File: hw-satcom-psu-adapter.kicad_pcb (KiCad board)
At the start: 2 copper layers, 148.9 x 85.2 mm, 87 parts, among them J1 XT60, J2 ATX-24, J3 Conn_02x02_Top_Bottom, J4 Conn_02x02_Top_Bottom, Q2 KIA3510AD, Q5 2N7002, Q6 2N7002, U1 Brick-DCDC, U10 ZXDN10, U2 LM5067, U3 EL3H7(B)(TA)-G, U4 EL3H7(B)(TA)-G, U5 AV10-48S05, U6 EL3H7(B)(TA)-G, U7 TPS3510, U8 ZXDN10, U9 ZXDN10

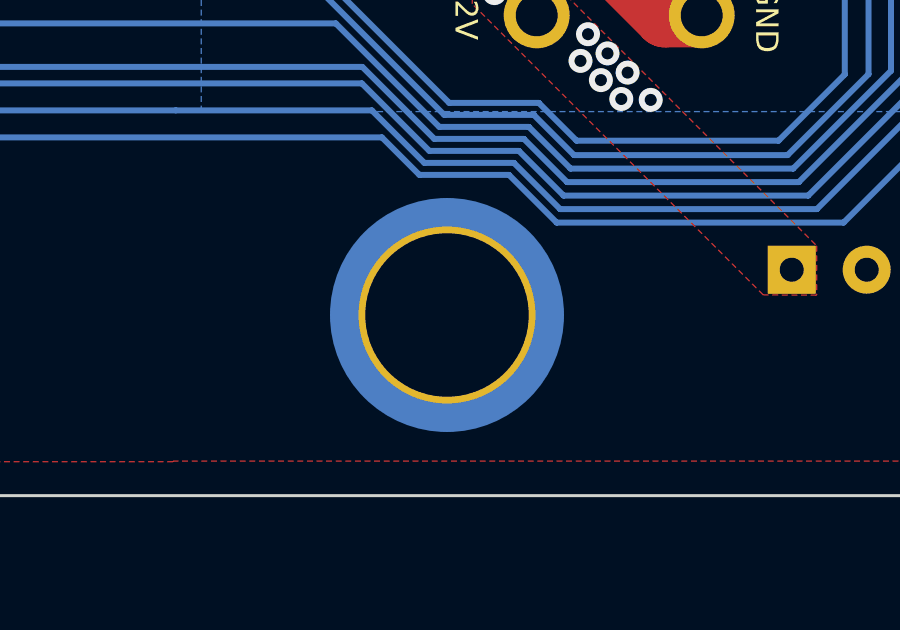
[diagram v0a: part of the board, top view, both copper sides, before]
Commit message: Adjust screw hole position
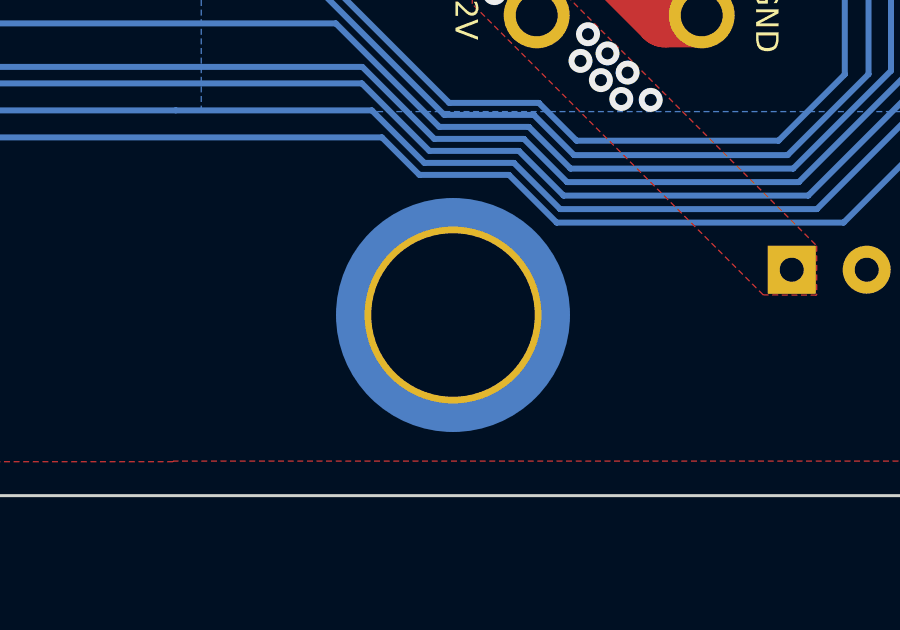
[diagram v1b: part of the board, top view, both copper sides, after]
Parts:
- moved H7 0.20 mm to (205.6, 129.7)
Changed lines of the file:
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@@
   )
   (footprint "t123yh:MountingHole_SMTSO-632" locked (layer "B.Cu")
-    (at 205.39 129.72 180)
+    (at 205.59 129.72 180)
     (descr "Screw Hole 6#32")
     (property "Sheetfile" "文件： hw-satcom-psu-adapter.kicad_sch")

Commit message: Reduce LED brightness
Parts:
- R14, R9: value 56k -> 68k
- R22: value 8.2k -> 10k
- R7, R8: value 5.1k -> 6.8k
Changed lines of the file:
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@@
       (effects (font (size 1 1) (thickness 0.15)))
     )
-    (fp_text value "56k" (at 0.136657 3.388724) (layer "F.Fab")
+    (fp_text value "68k" (at 0.136657 3.388724) (layer "F.Fab")
       (effects (font (size 1 1) (thickness 0.15)))
     )
@@
       (effects (font (size 1 1) (thickness 0.15)))
     )
-    (fp_text value "8.2k" (at 0.696657 3.173724 90) (layer "F.Fab")
+    (fp_text value "10k" (at 0.696657 3.173724 90) (layer "F.Fab")
       (effects (font (size 1 1) (thickness 0.15)))
     )
@@
       (effects (font (size 1 1) (thickness 0.15)))
     )
-    (fp_text value "5.1k" (at 0.696657 3.173724) (layer "F.Fab")
+    (fp_text value "6.8k" (at 0.696657 3.173724) (layer "F.Fab")
       (effects (font (size 1 1) (thickness 0.15)))
     )
@@
       (effects (font (size 1 1) (thickness 0.15)))
     )
-    (fp_text value "56k" (at 0.136657 3.388724 -270) (layer "F.Fab")
+    (fp_text value "68k" (at 0.136657 3.388724 -270) (layer "F.Fab")
       (effects (font (size 1 1) (thickness 0.15)))
     )
@@
       (effects (font (size 1 1) (thickness 0.15)))
     )
-    (fp_text value "5.1k" (at 0.696657 3.173724) (layer "F.Fab")
-      (effects (font (size 1 1) (thickness 0.15)))
-    )
+    (fp_text value "6.8k" (at 0.696657 3.173724) (layer "F.Fab")
+      (effects (font (size 1 1) (thickness 0.15)))
+    )

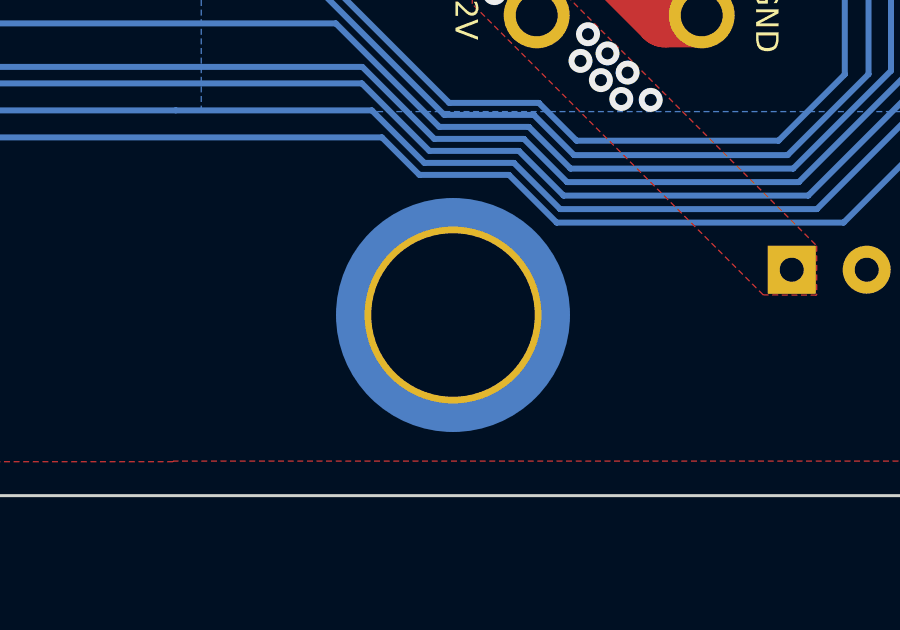
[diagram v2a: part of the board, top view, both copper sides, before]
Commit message: Revert "Adjust screw hole position"
This reverts commit 63cac71901258e286d442f6c161a0cf4eb18ce6f.
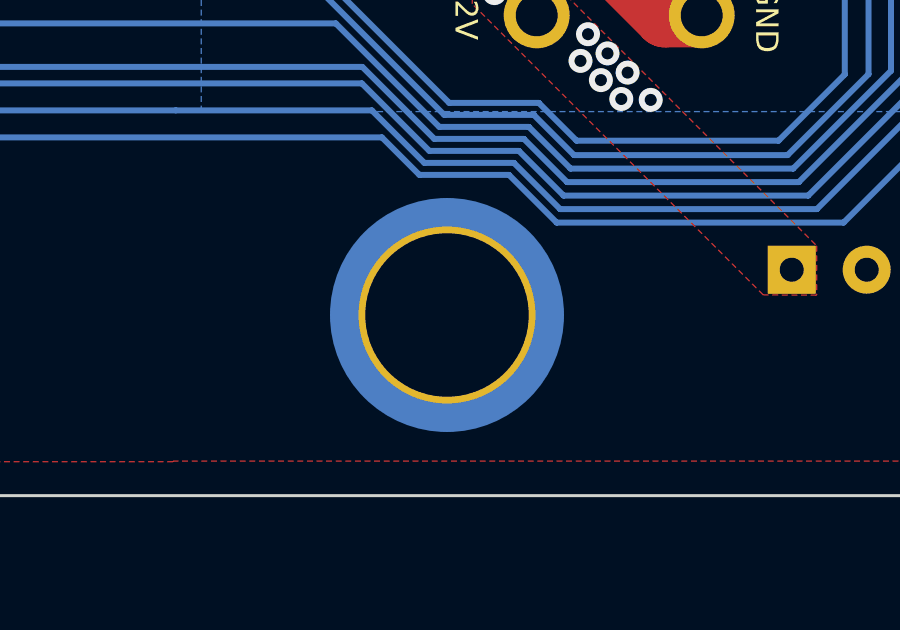
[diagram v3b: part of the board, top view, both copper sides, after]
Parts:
- moved H7 0.20 mm to (205.4, 129.7)
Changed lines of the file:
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@@
   )
   (footprint "t123yh:MountingHole_SMTSO-632" locked (layer "B.Cu")
-    (at 205.59 129.72 180)
+    (at 205.39 129.72 180)
     (descr "Screw Hole 6#32")
     (property "Sheetfile" "文件： hw-satcom-psu-adapter.kicad_sch")
